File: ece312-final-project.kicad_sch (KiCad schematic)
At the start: 4 parts, among them U1 ATmega328-P, Y1 32.768KHz Crystal

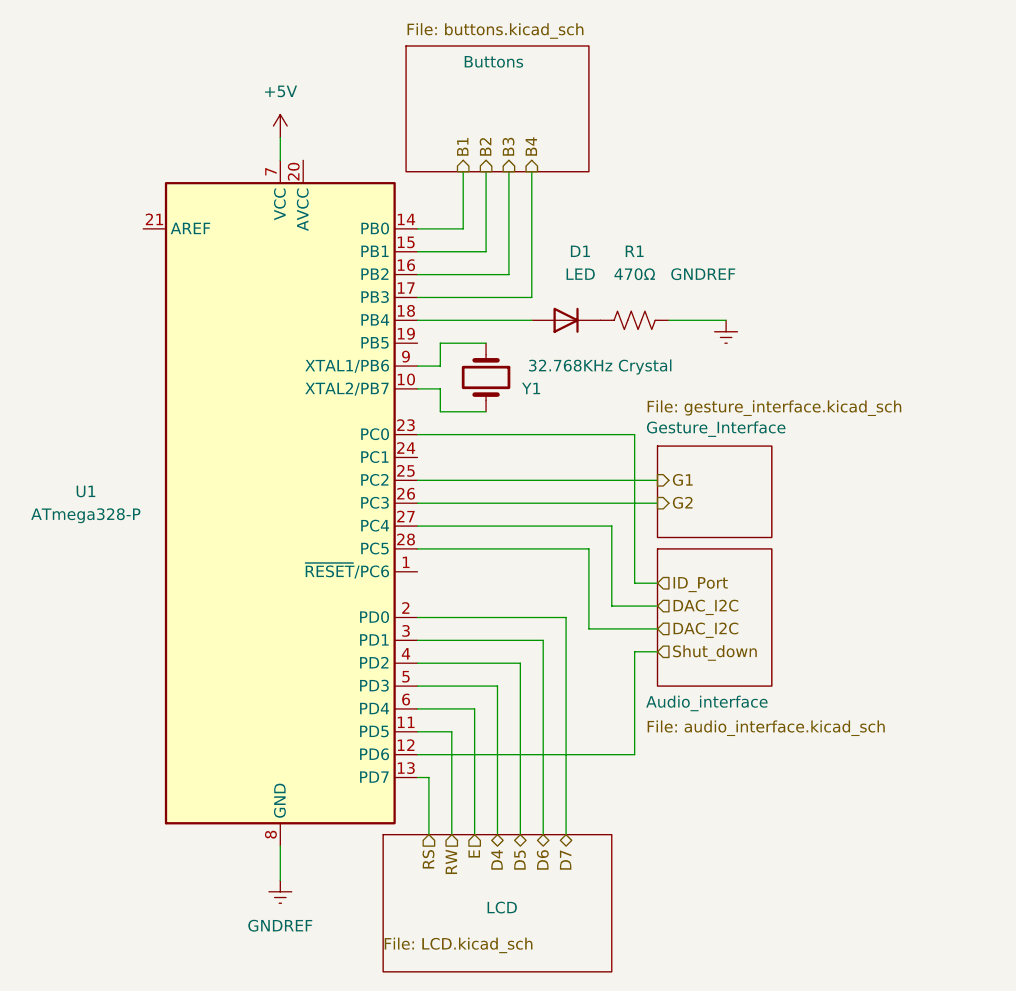
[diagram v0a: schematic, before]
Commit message: Added Gesture sensor and Audio system schematics and properly fixed port directions
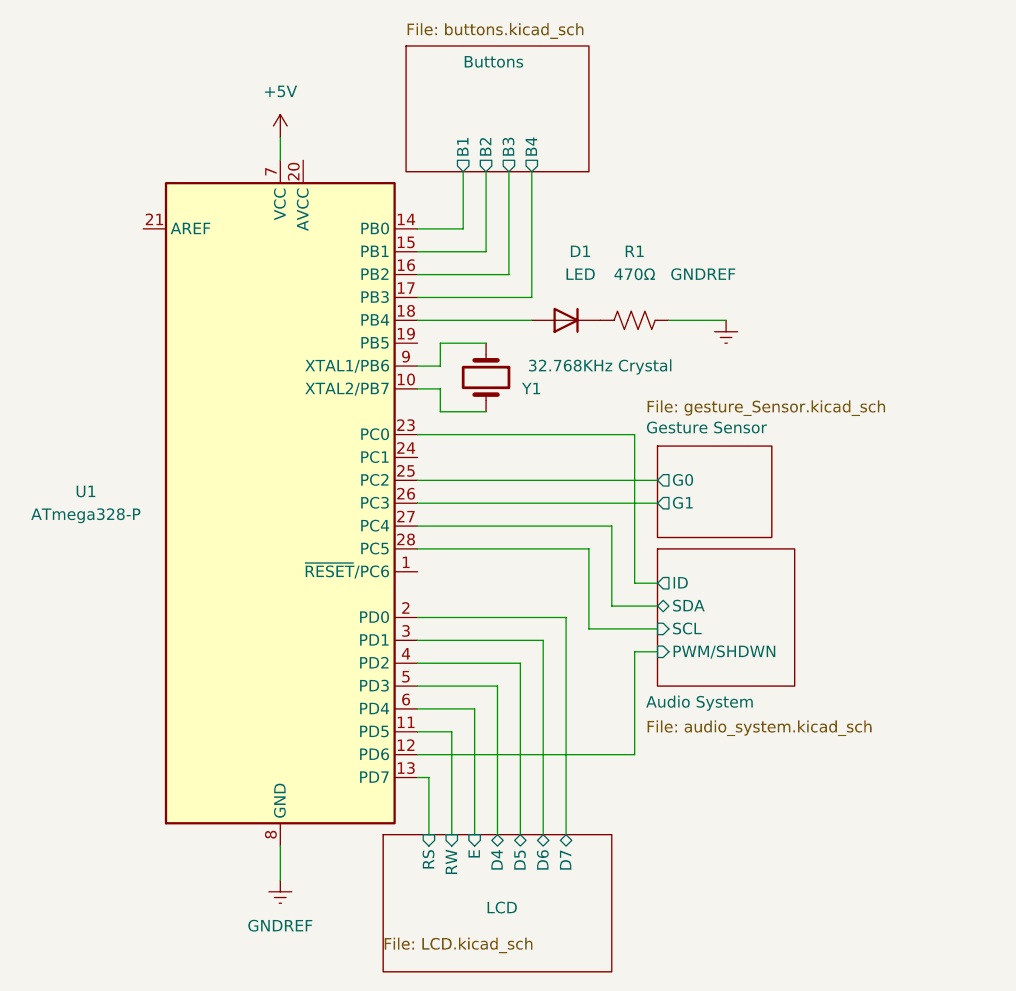
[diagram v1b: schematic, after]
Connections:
- net B1 renamed Buttons/B1
- net B2 renamed Buttons/B2
- net B3 renamed Buttons/B3
- net B4 renamed Buttons/B4
- net D4 renamed LCD/D4
- net D5 renamed LCD/D5
- net D6 renamed LCD/D6
- net D7 renamed LCD/D7
- net DAC_I2C renamed Audio System/SCL
- net Audio System/SCL: no longer U1.27 (PC4)
- net E renamed LCD/E
- net G1 renamed Gesture Sensor/G0
- net G2 renamed Gesture Sensor/G1
- net ID_Port renamed Audio System/ID
- net RS renamed LCD/RS
- net RW renamed LCD/RW
- net Shut_down renamed Audio System/PWM/SHDWN
- new net Audio System/SDA: U1.27 (PC4)
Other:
- sheet Audio_interface renamed Audio System
- sheet Gesture_Interface renamed Gesture Sensor
- sheet Audio System: file audio_interface.kicad_sch -> audio_system.kicad_sch
- sheet Audio System ports: added ID, PWM/SHDWN, SCL, SDA; removed none
- sheet Buttons ports: added B1, B2, B3, B4; removed none
- sheet Gesture Sensor: file gesture_interface.kicad_sch -> gesture_Sensor.kicad_sch
- sheet Gesture Sensor ports: added G0, G1; removed none
- sheet LCD ports: added D4, D5, D6, D7, E, RS, RW; removed none
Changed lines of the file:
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@@
     (stroke (width 0) (type default))
   )
-  (hierarchical_label "B1" (shape output) (at 153.67 58.42 90) (fields_autoplaced)
-    (effects (font (size 1.27 1.27)) (justify left))
-  )
-  (hierarchical_label "D4" (shape bidirectional) (at 157.48 132.08 270) (fields_autoplaced)
-    (effects (font (size 1.27 1.27)) (justify right))
-  )
-  (hierarchical_label "B3" (shape output) (at 158.75 58.42 90) (fields_autoplaced)
-    (effects (font (size 1.27 1.27)) (justify left))
-  )
-  (hierarchical_label "G2" (shape output) (at 175.26 95.25 0) (fields_autoplaced)
-    (effects (font (size 1.27 1.27)) (justify left))
-  )
-  (hierarchical_label "DAC_I2C" (shape input) (at 175.26 106.68 0) (fields_autoplaced)
-    (effects (font (size 1.27 1.27)) (justify left))
-  )
-  (hierarchical_label "ID_Port" (shape input) (at 175.26 104.14 0) (fields_autoplaced)
-    (effects (font (size 1.27 1.27)) (justify left))
-  )
-  (hierarchical_label "B4" (shape output) (at 161.29 58.42 90) (fields_autoplaced)
-    (effects (font (size 1.27 1.27)) (justify left))
-  )
-  (hierarchical_label "E" (shape input) (at 154.94 132.08 270) (fields_autoplaced)
-    (effects (font (size 1.27 1.27)) (justify right))
-  )
-  (hierarchical_label "G1" (shape output) (at 175.26 92.71 0) (fields_autoplaced)
-    (effects (font (size 1.27 1.27)) (justify left))
-  )
-  (hierarchical_label "D6" (shape bidirectional) (at 162.56 132.08 270) (fields_autoplaced)
-    (effects (font (size 1.27 1.27)) (justify right))
-  )
-  (hierarchical_label "D7" (shape bidirectional) (at 165.1 132.08 270) (fields_autoplaced)
-    (effects (font (size 1.27 1.27)) (justify right))
-  )
-  (hierarchical_label "DAC_I2C" (shape input) (at 175.26 109.22 0) (fields_autoplaced)
-    (effects (font (size 1.27 1.27)) (justify left))
-  )
-  (hierarchical_label "Shut_down" (shape input) (at 175.26 111.76 0) (fields_autoplaced)
-    (effects (font (size 1.27 1.27)) (justify left))
-  )
-  (hierarchical_label "B2" (shape output) (at 156.21 58.42 90) (fields_autoplaced)
-    (effects (font (size 1.27 1.27)) (justify left))
-  )
-  (hierarchical_label "D5" (shape bidirectional) (at 160.02 132.08 270) (fields_autoplaced)
-    (effects (font (size 1.27 1.27)) (justify right))
-  )
-  (hierarchical_label "RW" (shape input) (at 152.4 132.08 270) (fields_autoplaced)
-    (effects (font (size 1.27 1.27)) (justify right))
-  )
-  (hierarchical_label "RS" (shape input) (at 149.86 132.08 270) (fields_autoplaced)
-    (effects (font (size 1.27 1.27)) (justify right))
-  )
   (symbol (lib_id "power:GNDREF") (at 182.88 74.93 0) (unit 1)
     (in_bom yes) (on_board yes) (dnp no)
-    (property "Reference" "#PWR?" (at 182.88 81.28 0)
+    (property "Reference" "#PWR03" (at 182.88 81.28 0)
       (effects (font (size 1.27 1.27)) hide)
     )
@@
       (project "ece312-final-project"
         (path "/fafbac94-05bd-4749-8502-4886ccc0ec35"
-          (reference "#PWR?") (unit 1)
+          (reference "#PWR03") (unit 1)
         )
       )
@@
   (symbol (lib_id "power:+5V") (at 133.35 54.61 0) (unit 1)
     (in_bom yes) (on_board yes) (dnp no) (fields_autoplaced)
-    (property "Reference" "#PWR?" (at 133.35 58.42 0)
+    (property "Reference" "#PWR01" (at 133.35 58.42 0)
       (effects (font (size 1.27 1.27)) hide)
     )
@@
       (project "ece312-final-project"
         (path "/fafbac94-05bd-4749-8502-4886ccc0ec35"
-          (reference "#PWR?") (unit 1)
+          (reference "#PWR01") (unit 1)
         )
       )
@@
   (symbol (lib_id "power:GNDREF") (at 133.35 137.16 0) (unit 1)
     (in_bom yes) (on_board yes) (dnp no) (fields_autoplaced)
-    (property "Reference" "#PWR?" (at 133.35 143.51 0)
+    (property "Reference" "#PWR02" (at 133.35 143.51 0)
       (effects (font (size 1.27 1.27)) hide)
     )
@@
       (project "ece312-final-project"
         (path "/fafbac94-05bd-4749-8502-4886ccc0ec35"
-          (reference "#PWR?") (unit 1)
+          (reference "#PWR02") (unit 1)
         )
       )
@@
     )
   )
-  (sheet (at 175.26 100.33) (size 12.7 15.24)
-    (stroke (width 0.1524) (type solid))
-    (fill (color 0 0 0 0.0000))
-    (property "Sheetname" "Audio_interface" (at 173.99 118.11 0)
-      (effects (font (size 1.27 1.27)) (justify left bottom))
-    )
-    (property "Sheetfile" "audio_interface.kicad_sch" (at 173.99 119.38 0)
-      (effects (font (size 1.27 1.27)) (justify left top))
+  (sheet (at 175.26 100.33) (size 15.24 15.24)
+    (stroke (width 0.1524) (type solid))
+    (fill (color 0 0 0 0.0000))
+    (property "Sheetname" "Audio System" (at 173.99 118.11 0)
+      (effects (font (size 1.27 1.27)) (justify left bottom))
+    )
+    (property "Sheetfile" "audio_system.kicad_sch" (at 173.99 119.38 0)
+      (effects (font (size 1.27 1.27)) (justify left top))
+    )
+    (pin "SCL" input (at 175.26 109.22 180)
+      (effects (font (size 1.27 1.27)) (justify left))
+    )
+    (pin "SDA" bidirectional (at 175.26 106.68 180)
+      (effects (font (size 1.27 1.27)) (justify left))
+    )
+    (pin "PWM{slash}SHDWN" input (at 175.26 111.76 180)
+      (effects (font (size 1.27 1.27)) (justify left))
+    )
+    (pin "ID" output (at 175.26 104.14 180)
+      (effects (font (size 1.27 1.27)) (justify left))
     )
     (instances
@@
       (effects (font (size 1.27 1.27)) (justify left top))
     )
+    (pin "D4" bidirectional (at 157.48 132.08 90)
+      (effects (font (size 1.27 1.27)) (justify right))
+    )
+    (pin "RS" input (at 149.86 132.08 90)
+      (effects (font (size 1.27 1.27)) (justify right))
+    )
+    (pin "E" input (at 154.94 132.08 90)
+      (effects (font (size 1.27 1.27)) (justify right))
+    )
+    (pin "RW" input (at 152.4 132.08 90)
+      (effects (font (size 1.27 1.27)) (justify right))
+    )
+    (pin "D6" bidirectional (at 162.56 132.08 90)
+      (effects (font (size 1.27 1.27)) (justify right))
+    )
+    (pin "D5" bidirectional (at 160.02 132.08 90)
+      (effects (font (size 1.27 1.27)) (justify right))
+    )
+    (pin "D7" bidirectional (at 165.1 132.08 90)
+      (effects (font (size 1.27 1.27)) (justify right))
+    )
     (instances
       (project "ece312-final-project"
@@
       (effects (font (size 1.27 1.27)) (justify left top))
     )
+    (pin "B4" output (at 161.29 58.42 270)
+      (effects (font (size 1.27 1.27)) (justify left))
+    )
+    (pin "B3" output (at 158.75 58.42 270)
+      (effects (font (size 1.27 1.27)) (justify left))
+    )
+    (pin "B1" output (at 153.67 58.42 270)
+      (effects (font (size 1.27 1.27)) (justify left))
+    )
+    (pin "B2" output (at 156.21 58.42 270)
+      (effects (font (size 1.27 1.27)) (justify left))
+    )
     (instances
       (project "ece312-final-project"
@@
     (stroke (width 0.1524) (type solid))
     (fill (color 0 0 0 0.0000))
-    (property "Sheetname" "Gesture_Interface" (at 173.99 87.63 0)
-      (effects (font (size 1.27 1.27)) (justify left bottom))
-    )
-    (property "Sheetfile" "gesture_interface.kicad_sch" (at 173.99 83.82 0)
-      (effects (font (size 1.27 1.27)) (justify left top))
-    )
-    (instances
+    (property "Sheetname" "Gesture Sensor" (at 173.99 87.63 0)
+      (effects (font (size 1.27 1.27)) (justify left bottom))
+    )
+    (property "Sheetfile" "gesture_Sensor.kicad_sch" (at 173.99 83.82 0)
+      (effects (font (size 1.27 1.27)) (justify left top))
+    )
+    (pin "G0" output (at 175.26 92.71 180)
+      (effects (font (size 1.27 1.27)) (justify left))
+    )
+    (pin "G1" output (at 175.26 95.25 180)
+      (effects (font (size 1.27 1.27)) (justify left))
+    )
+    (instances
